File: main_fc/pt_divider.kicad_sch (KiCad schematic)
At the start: 4 parts

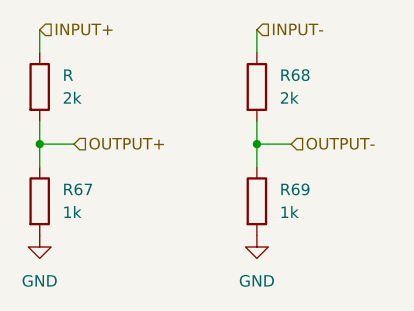
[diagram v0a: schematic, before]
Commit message: added new stm symbol/footprint
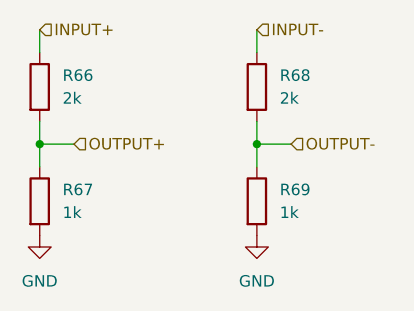
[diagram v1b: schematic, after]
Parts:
- renumbered R to R66
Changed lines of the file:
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@@
 		(dnp no)
 		(fields_autoplaced yes)
-		(property "Reference" "#PWR080"
+		(property "Reference" "#PWR0143"
 			(at 93.98 76.2 0)
 			(effects
@@
 			(project "main_fc"
 				(path "/2e5bfe72-277e-40a6-babb-0928c11aa964/0623c7a4-3489-48a8-b4fd-fc769b8a46ae"
-					(reference "#PWR082")
+					(reference "#PWR0145")
 					(unit 1)
 				)
 				(path "/2e5bfe72-277e-40a6-babb-0928c11aa964/5b77ee74-a914-43f5-b3e4-ef71a6a6a535"
-					(reference "#PWR084")
+					(reference "#PWR0147")
 					(unit 1)
 				)
@@
 				)
 				(path "/2e5bfe72-277e-40a6-babb-0928c11aa964/f29c1d9b-cdd1-433a-929a-0c43887a2918"
-					(reference "#PWR080")
+					(reference "#PWR0143")
 					(unit 1)
 				)
 				(path "/2e5bfe72-277e-40a6-babb-0928c11aa964/f6855efb-35f7-496d-9fa9-30d71d922eaa"
+					(reference "#PWR0157")
+					(unit 1)
+				)
+				(path "/2e5bfe72-277e-40a6-babb-0928c11aa964/fa3bc39c-2863-4d9d-813a-0640fc4bb220"
 					(reference "#PWR0155")
-					(unit 1)
-				)
-				(path "/2e5bfe72-277e-40a6-babb-0928c11aa964/fa3bc39c-2863-4d9d-813a-0640fc4bb220"
-					(reference "#PWR0157")
 					(unit 1)
 				)
@@
 		(dnp no)
 		(fields_autoplaced yes)
-		(property "Reference" "#PWR"
+		(property "Reference" "#PWR0142"
 			(at 69.85 76.2 0)
 			(effects
@@
 			(project "main_fc"
 				(path "/2e5bfe72-277e-40a6-babb-0928c11aa964/0623c7a4-3489-48a8-b4fd-fc769b8a46ae"
-					(reference "#PWR081")
+					(reference "#PWR0144")
 					(unit 1)
 				)
 				(path "/2e5bfe72-277e-40a6-babb-0928c11aa964/5b77ee74-a914-43f5-b3e4-ef71a6a6a535"
-					(reference "#PWR083")
+					(reference "#PWR0146")
 					(unit 1)
 				)
@@
 					(unit 1)
 				)
+				(path "/2e5bfe72-277e-40a6-babb-0928c11aa964/f29c1d9b-cdd1-433a-929a-0c43887a2918"
+					(reference "#PWR0142")
+					(unit 1)
+				)
 				(path "/2e5bfe72-277e-40a6-babb-0928c11aa964/f6855efb-35f7-496d-9fa9-30d71d922eaa"
+					(reference "#PWR0156")
+					(unit 1)
+				)
+				(path "/2e5bfe72-277e-40a6-babb-0928c11aa964/fa3bc39c-2863-4d9d-813a-0640fc4bb220"
 					(reference "#PWR0154")
-					(unit 1)
-				)
-				(path "/2e5bfe72-277e-40a6-babb-0928c11aa964/fa3bc39c-2863-4d9d-813a-0640fc4bb220"
-					(reference "#PWR0156")
 					(unit 1)
 				)
@@
 				)
 				(path "/2e5bfe72-277e-40a6-babb-0928c11aa964/f6855efb-35f7-496d-9fa9-30d71d922eaa"
+					(reference "R97")
+					(unit 1)
+				)
+				(path "/2e5bfe72-277e-40a6-babb-0928c11aa964/fa3bc39c-2863-4d9d-813a-0640fc4bb220"
 					(reference "R93")
-					(unit 1)
-				)
-				(path "/2e5bfe72-277e-40a6-babb-0928c11aa964/fa3bc39c-2863-4d9d-813a-0640fc4bb220"
-					(reference "R97")
 					(unit 1)
 				)
@@
 				)
 				(path "/2e5bfe72-277e-40a6-babb-0928c11aa964/f6855efb-35f7-496d-9fa9-30d71d922eaa"
+					(reference "R96")
+					(unit 1)
+				)
+				(path "/2e5bfe72-277e-40a6-babb-0928c11aa964/fa3bc39c-2863-4d9d-813a-0640fc4bb220"
 					(reference "R92")
-					(unit 1)
-				)
-				(path "/2e5bfe72-277e-40a6-babb-0928c11aa964/fa3bc39c-2863-4d9d-813a-0640fc4bb220"
-					(reference "R96")
 					(unit 1)
 				)
@@
 				)
 				(path "/2e5bfe72-277e-40a6-babb-0928c11aa964/f6855efb-35f7-496d-9fa9-30d71d922eaa"
+					(reference "R95")
+					(unit 1)
+				)
+				(path "/2e5bfe72-277e-40a6-babb-0928c11aa964/fa3bc39c-2863-4d9d-813a-0640fc4bb220"
 					(reference "R91")
-					(unit 1)
-				)
-				(path "/2e5bfe72-277e-40a6-babb-0928c11aa964/fa3bc39c-2863-4d9d-813a-0640fc4bb220"
-					(reference "R95")
 					(unit 1)
 				)
@@
 		(dnp no)
 		(fields_autoplaced yes)
-		(property "Reference" "R"
+		(property "Reference" "R66"
 			(at 72.39 52.0699 0)
 			(effects
@@
 					(unit 1)
 				)
+				(path "/2e5bfe72-277e-40a6-babb-0928c11aa964/f29c1d9b-cdd1-433a-929a-0c43887a2918"
+					(reference "R66")
+					(unit 1)
+				)
 				(path "/2e5bfe72-277e-40a6-babb-0928c11aa964/f6855efb-35f7-496d-9fa9-30d71d922eaa"
+					(reference "R94")
+					(unit 1)
+				)
+				(path "/2e5bfe72-277e-40a6-babb-0928c11aa964/fa3bc39c-2863-4d9d-813a-0640fc4bb220"
 					(reference "R90")
 					(unit 1)
 				)
-				(path "/2e5bfe72-277e-40a6-babb-0928c11aa964/fa3bc39c-2863-4d9d-813a-0640fc4bb220"
-					(reference "R94")
-					(unit 1)
-				)
